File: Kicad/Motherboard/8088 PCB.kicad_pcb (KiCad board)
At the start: 4 copper layers, 177.8 x 106.7 mm, 80 parts, among them J1 Bus_ISA_8bit, J2 Mini-DIN-6, J3 SPK, J4 CS7, SW1 RESET, U1 8088, U10 8237, U11 74LS573, U12 74LS139, U13 AS6C4008, U14 AS6C1008, U15 27C512, U16 74LS138, U17 8284, U18 74LS74, U19 W83C42P, U2 74LS573, U20 74LS07, U21 74LS04, U22 8284, U23 74LS245, U24 74LS573, U25 74LS126, U26 74LS125, U3 74LS573, U4 74LS245, U5 8254, U6 8259, U7 74LS670, U8 74LS257, U9 27C512, Y1 14.31818, Y2 CRYSTAL

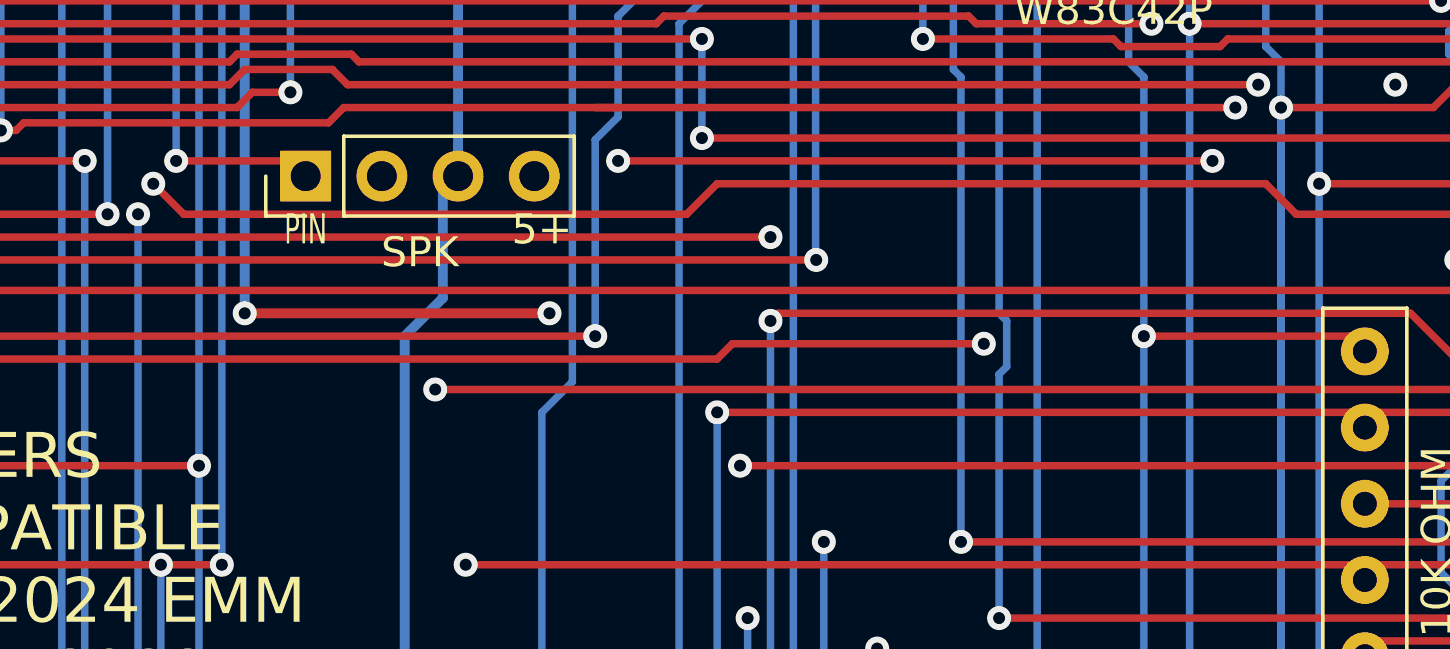
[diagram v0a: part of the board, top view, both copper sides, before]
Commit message: Update IRQ 1 pin
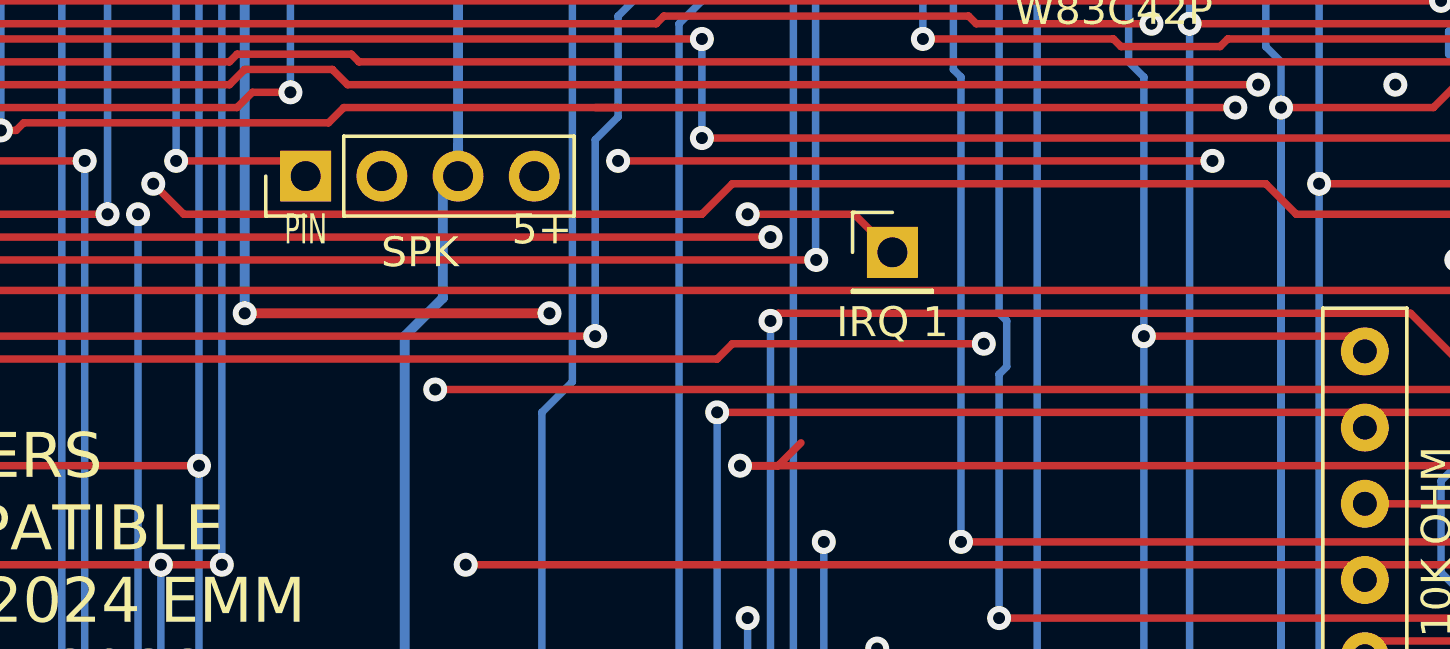
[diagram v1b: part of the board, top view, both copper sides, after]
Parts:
- added J5: IRQ 1, Connector_PinHeader_2.54mm:PinHeader_1x01_P2.54mm_Vertical, F.Cu at (179.3, 75.4)
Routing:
- net /IRQ1: track 102.8 -> 108.2 mm, vias 4 -> 5
- net /DACK1: track 107.3 -> 109.6 mm
- net /A7: track 289.1 -> 289.7 mm

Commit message: update adapter
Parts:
- moved J5 35.1 mm to (178.3, 40.4)
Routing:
- net /IRQ1: track 108.2 -> 121.4 mm
- net /RESOUT: track 207.7 -> 206.8 mm
- net /A7: track 289.7 -> 289.1 mm

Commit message: Update
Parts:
- U11, U2, U24, U3: value 74LS573 -> 74*573
- U12: value 74LS139 -> 74*139
- U16: value 74LS138 -> 74*138
- U18: value 74LS74 -> 74*74
- U19: value W83C42P -> 82C42
- U20: value 74LS07 -> 74*07
- U21: value 74LS04 -> 74*04
- U23, U4: value 74LS245 -> 74*245
- U25: value 74LS126 -> 74*126
- U26: value 74LS125 -> 74*125
- U7: value 74LS670 -> 74*670
- U8: value 74LS257 -> 74*257
- moved R 0.13 mm to (230.9, 133.2)
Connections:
- J2 pad : /GND -> (no net)
- R pad 1: /GND -> (no net)
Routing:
- net /GND: track 1195.2 -> 1184.8 mm
- net /DACK1: track 109.6 -> 108.6 mm
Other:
- board text added: "D0 - 8237 D1 - 8259 D2 - 8254 D3 - 8242 D4 - PORT 61 D5 - 74*670 D6 - NC D7 - CS7"
